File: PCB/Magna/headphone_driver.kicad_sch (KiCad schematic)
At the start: 36 parts, among them J1201 AudioJack3, U1201 NE5532, U1202 NE5532, U1203 TDA2822D

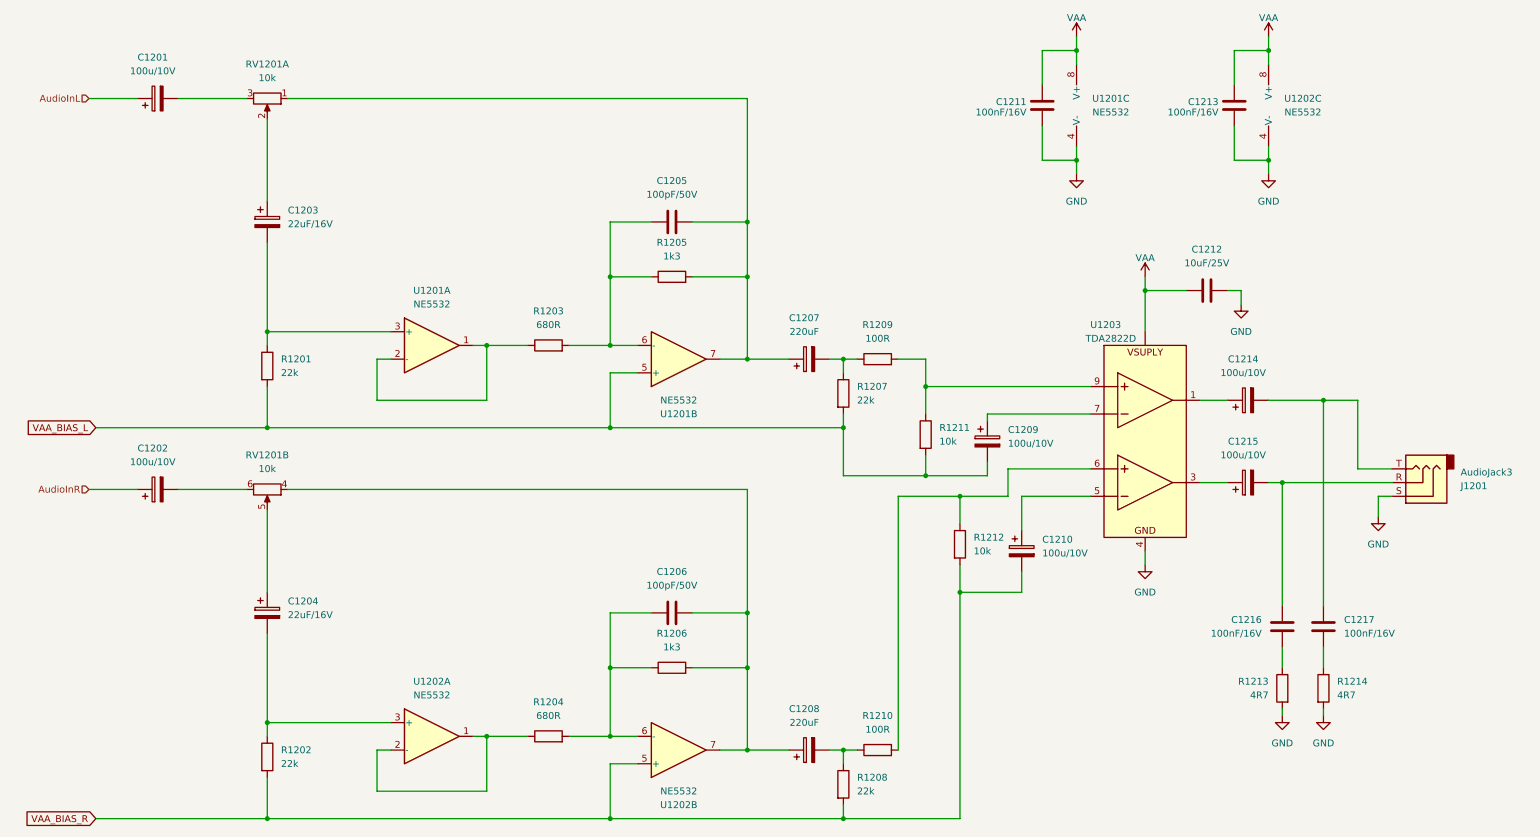
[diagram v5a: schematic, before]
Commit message: Add even more component footprints and partnumbers
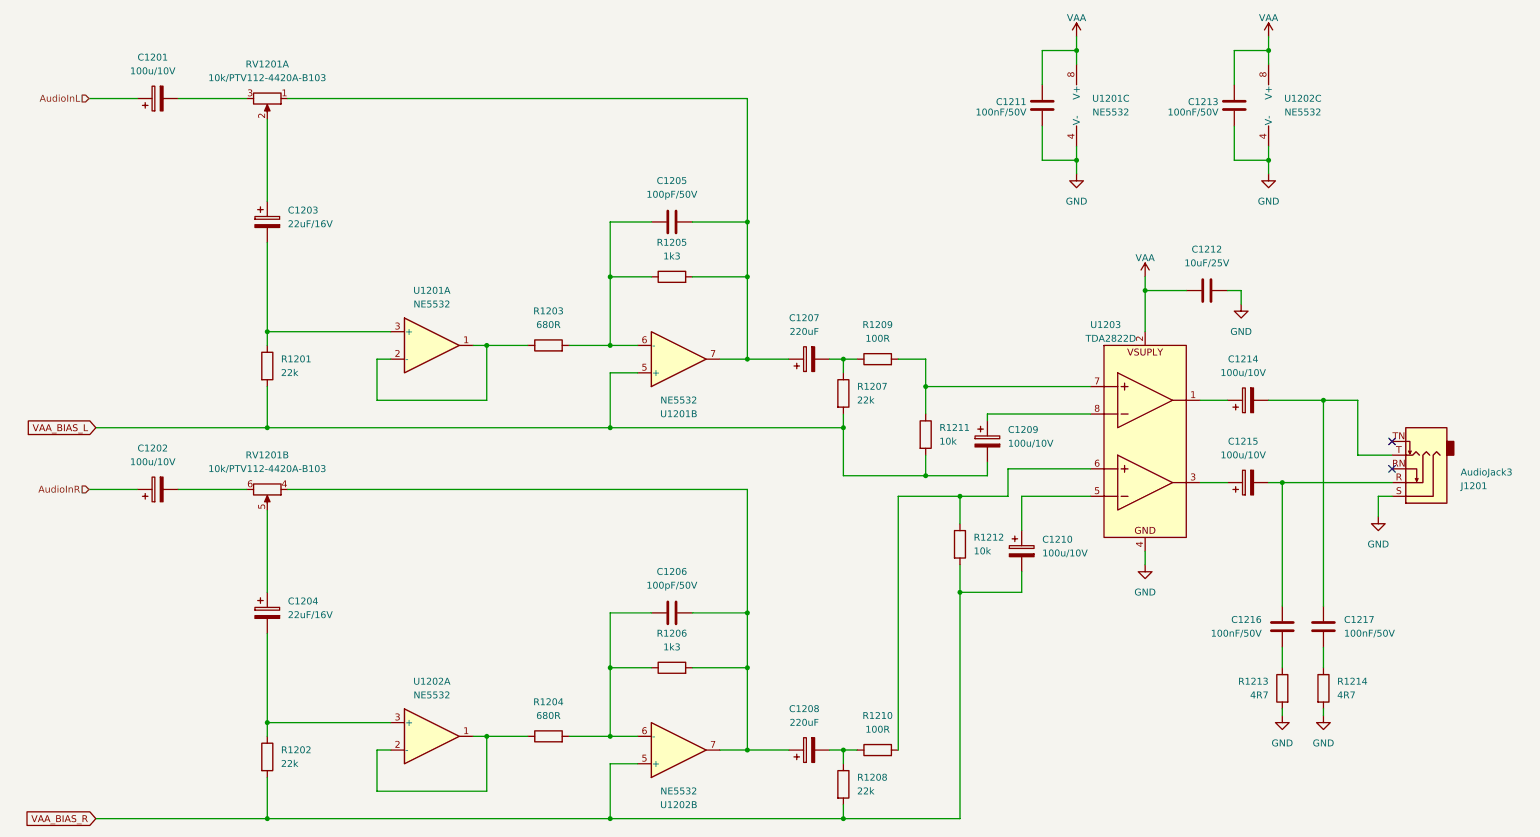
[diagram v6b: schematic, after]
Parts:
- C1205, C1206: footprint Capacitor_SMD:C_0805_2012Metric -> Capacitor_SMD:C_0805_2012Metric_Pad1.18x1.45mm_HandSolder
- C1211, C1213, C1216, C1217: value 100nF/16V -> 100nF/50V; footprint Capacitor_SMD:C_0805_2012Metric -> Capacitor_SMD:C_0805_2012Metric_Pad1.18x1.45mm_HandSolder; LCSC C218638 -> C49678
- J1201: symbol Connector_Audio:AudioJack3 -> Connector_Audio:AudioJack3_SwitchTR
- R1201, R1202, R1207, R1208, R1211, R1212: footprint Resistor_SMD:R_0805_2012Metric -> Resistor_SMD:R_0805_2012Metric_Pad1.20x1.40mm_HandSolder
- RV1201: value 10k -> 10k/PTV112-4420A-B103; footprint (none) -> Skrooter_footprints:Potentiometer_Bourns_PTV09A-1_Dual_Vertical
- U1201, U1202: footprint (none) -> Package_SO:SOIC-8_3.9x4.9mm_P1.27mm
- U1203: footprint (none) -> Package_SO:SOP-8_3.9x4.9mm_P1.27mm
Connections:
- net VAA: now also U1203.2 (VCC); no longer U1203. (VCC)
- net at C1209.1: now also U1203.8 (Input1+); no longer U1203.7 (Input1+)
- net at R1209.2, R1211.1: now also U1203.7 (Input1-); no longer U1203.9 (Input1-)
- no-connect marks 0 -> 2
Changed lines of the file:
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@@
   (junction (at 121.92 78.74) (diameter 0) (color 0 0 0 0)
   )
+  (no_connect (at 266.7 101.6))
+  (no_connect (at 266.7 96.52))
   (wire (pts (xy 62.23 33.02) (xy 147.32 33.02))
     (stroke (width 0) (type default))
@@
     (stroke (width 0) (type default))
   )
-  (wire (pts (xy 266.7 101.6) (xy 260.35 101.6))
-    (stroke (width 0) (type default))
-  )
   (wire (pts (xy 41.91 33.02) (xy 54.61 33.02))
     (stroke (width 0) (type default))
@@
     (stroke (width 0) (type default))
   )
-  (wire (pts (xy 260.35 88.9) (xy 260.35 101.6))
+  (wire (pts (xy 260.35 88.9) (xy 260.35 99.06))
     (stroke (width 0) (type default))
   )
@@
   )
   (wire (pts (xy 195.58 106.68) (xy 186.69 106.68))
+    (stroke (width 0) (type default))
+  )
+  (wire (pts (xy 260.35 99.06) (xy 266.7 99.06))
     (stroke (width 0) (type default))
   )
@@
       (effects (font (size 1.27 1.27)))
     )
-    (property "Value" "10k" (at 58.42 101.6 90)
-      (effects (font (size 1.27 1.27)))
-    )
-    (property "Footprint" "" (at 58.42 105.41 0)
+    (property "Value" "10k/PTV112-4420A-B103" (at 58.42 101.6 90)
+      (effects (font (size 1.27 1.27)))
+    )
+    (property "Footprint" "Skrooter_footprints:Potentiometer_Bourns_PTV09A-1_Dual_Vertical" (at 58.42 105.41 0)
       (effects (font (size 1.27 1.27)) hide)
     )
@@
     )
   )
-  (symbol (lib_id "Connector_Audio:AudioJack3") (at 271.78 104.14 180) (unit 1)
+  (symbol (lib_id "Connector_Audio:AudioJack3_SwitchTR") (at 271.78 104.14 180) (unit 1)
     (in_bom yes) (on_board yes) (dnp no)
     (property "Reference" "J1201" (at 279.4 104.775 0)
@@
     (pin "R")
     (pin "S")
+    (pin "RN")
+    (pin "TN")
     (instances
       (project "Magna"
@@
       (effects (font (size 1.27 1.27)) (justify left))
     )
-    (property "Footprint" "Resistor_SMD:R_0805_2012Metric" (at 56.642 82.55 90)
+    (property "Footprint" "Resistor_SMD:R_0805_2012Metric_Pad1.20x1.40mm_HandSolder" (at 56.642 82.55 90)
       (effects (font (size 1.27 1.27)) hide)
     )
@@
       (effects (font (size 1.27 1.27)))
     )
-    (property "Footprint" "" (at 88.9 78.74 0)
+    (property "Footprint" "Package_SO:SOIC-8_3.9x4.9mm_P1.27mm" (at 88.9 78.74 0)
       (effects (font (size 1.27 1.27)) hide)
     )
@@
       (effects (font (size 1.27 1.27)))
     )
-    (property "Value" "10k" (at 58.42 29.21 90)
-      (effects (font (size 1.27 1.27)))
-    )
-    (property "Footprint" "" (at 58.42 33.02 0)
+    (property "Value" "10k/PTV112-4420A-B103" (at 58.42 29.21 90)
+      (effects (font (size 1.27 1.27)))
+    )
+    (property "Footprint" "Skrooter_footprints:Potentiometer_Bourns_PTV09A-1_Dual_Vertical" (at 58.42 33.02 0)
       (effects (font (size 1.27 1.27)) hide)
     )
@@
       (effects (font (size 1.27 1.27)))
     )
-    (property "Footprint" "" (at 134.62 153.67 0)
+    (property "Footprint" "Package_SO:SOIC-8_3.9x4.9mm_P1.27mm" (at 134.62 153.67 0)
       (effects (font (size 1.27 1.27)) hide)
     )
@@
       (effects (font (size 1.27 1.27)) (justify left))
     )
-    (property "Footprint" "Resistor_SMD:R_0805_2012Metric" (at 163.322 87.63 90)
+    (property "Footprint" "Resistor_SMD:R_0805_2012Metric_Pad1.20x1.40mm_HandSolder" (at 163.322 87.63 90)
       (effects (font (size 1.27 1.27)) hide)
     )
@@
       (effects (font (size 1.27 1.27)) (justify left))
     )
-    (property "Footprint" "Resistor_SMD:R_0805_2012Metric" (at 163.322 160.02 90)
+    (property "Footprint" "Resistor_SMD:R_0805_2012Metric_Pad1.20x1.40mm_HandSolder" (at 163.322 160.02 90)
       (effects (font (size 1.27 1.27)) hide)
     )
@@
       (effects (font (size 1.27 1.27)) (justify left))
     )
-    (property "Footprint" "Resistor_SMD:R_0805_2012Metric" (at 184.912 115.57 90)
+    (property "Footprint" "Resistor_SMD:R_0805_2012Metric_Pad1.20x1.40mm_HandSolder" (at 184.912 115.57 90)
       (effects (font (size 1.27 1.27)) hide)
     )
@@
       (effects (font (size 1.27 1.27)) (justify left))
     )
-    (property "Footprint" "Resistor_SMD:R_0805_2012Metric" (at 56.642 154.94 90)
+    (property "Footprint" "Resistor_SMD:R_0805_2012Metric_Pad1.20x1.40mm_HandSolder" (at 56.642 154.94 90)
       (effects (font (size 1.27 1.27)) hide)
     )
@@
       (effects (font (size 1.27 1.27)))
     )
-    (property "Footprint" "" (at 134.62 81.28 0)
+    (property "Footprint" "Package_SO:SOIC-8_3.9x4.9mm_P1.27mm" (at 134.62 81.28 0)
       (effects (font (size 1.27 1.27)) hide)
     )
@@
       (effects (font (size 1.27 1.27)))
     )
-    (property "Footprint" "Capacitor_SMD:C_0805_2012Metric" (at 137.16 54.9148 0)
+    (property "Footprint" "Capacitor_SMD:C_0805_2012Metric_Pad1.18x1.45mm_HandSolder" (at 137.16 54.9148 0)
       (effects (font (size 1.27 1.27)) hide)
     )
@@
       (effects (font (size 1.27 1.27)))
     )
-    (property "Footprint" "" (at 246.38 34.29 0)
+    (property "Footprint" "Package_SO:SOIC-8_3.9x4.9mm_P1.27mm" (at 246.38 34.29 0)
       (effects (font (size 1.27 1.27)) hide)
     )
@@
       (effects (font (size 1.27 1.27)))
     )
-    (property "Footprint" "Capacitor_SMD:C_0805_2012Metric" (at 137.16 127.3048 0)
+    (property "Footprint" "Capacitor_SMD:C_0805_2012Metric_Pad1.18x1.45mm_HandSolder" (at 137.16 127.3048 0)
       (effects (font (size 1.27 1.27)) hide)
     )
@@
       (effects (font (size 1.27 1.27)) (justify left))
     )
-    (property "Footprint" "Resistor_SMD:R_0805_2012Metric" (at 178.562 95.25 90)
+    (property "Footprint" "Resistor_SMD:R_0805_2012Metric_Pad1.20x1.40mm_HandSolder" (at 178.562 95.25 90)
       (effects (font (size 1.27 1.27)) hide)
     )
@@
       (effects (font (size 1.27 1.27)))
     )
-    (property "Footprint" "" (at 210.82 34.29 0)
+    (property "Footprint" "Package_SO:SOIC-8_3.9x4.9mm_P1.27mm" (at 210.82 34.29 0)
       (effects (font (size 1.27 1.27)) hide)
     )
@@
       (effects (font (size 1.27 1.27)) (justify left))
     )
-    (property "Value" "100nF/16V" (at 242.57 132.08 0)
-      (effects (font (size 1.27 1.27)) (justify left))
-    )
-    (property "Footprint" "Capacitor_SMD:C_0805_2012Metric" (at 245.4148 134.62 0)
+    (property "Value" "100nF/50V" (at 242.57 132.08 0)
+      (effects (font (size 1.27 1.27)) (justify left))
+    )
+    (property "Footprint" "Capacitor_SMD:C_0805_2012Metric_Pad1.18x1.45mm_HandSolder" (at 245.4148 134.62 0)
       (effects (font (size 1.27 1.27)) hide)
     )
@@
       (effects (font (size 1.27 1.27)) hide)
     )
-    (property "LCSC" "C218638" (at 246.38 130.81 0)
+    (property "LCSC" "C49678" (at 246.38 130.81 0)
       (effects (font (size 1.27 1.27)) hide)
     )
@@
       (effects (font (size 1.27 1.27)) (justify left))
     )
-    (property "Value" "100nF/16V" (at 199.009 35.5673 0)
-      (effects (font (size 1.27 1.27)) (justify left))
-    )
-    (property "Footprint" "Capacitor_SMD:C_0805_2012Metric" (at 200.9648 38.1 0)
+    (property "Value" "100nF/50V" (at 199.009 35.5673 0)
+      (effects (font (size 1.27 1.27)) (justify left))
+    )
+    (property "Footprint" "Capacitor_SMD:C_0805_2012Metric_Pad1.18x1.45mm_HandSolder" (at 200.9648 38.1 0)
       (effects (font (size 1.27 1.27)) hide)
     )
@@
       (effects (font (size 1.27 1.27)) hide)
     )
-    (property "LCSC" "C218638" (at 201.93 34.29 0)
+    (property "LCSC" "C49678" (at 201.93 34.29 0)
       (effects (font (size 1.27 1.27)) hide)
     )
@@
       (effects (font (size 1.27 1.27)))
     )
-    (property "Footprint" "" (at 213.36 86.36 0)
+    (property "Footprint" "Package_SO:SOP-8_3.9x4.9mm_P1.27mm" (at 213.36 86.36 0)
       (effects (font (size 1.27 1.27)) hide)
     )
@@
     (pin "1")
     (pin "4")
-    (pin "")
+    (pin "2")
     (pin "7")
-    (pin "9")
+    (pin "8")
     (pin "3")
     (pin "5")
@@
       (effects (font (size 1.27 1.27)) (justify left))
     )
-    (property "Value" "100nF/16V" (at 257.81 132.08 0)
-      (effects (font (size 1.27 1.27)) (justify left))
-    )
-    (property "Footprint" "Capacitor_SMD:C_0805_2012Metric" (at 254.9652 134.62 0)
+    (property "Value" "100nF/50V" (at 257.81 132.08 0)
+      (effects (font (size 1.27 1.27)) (justify left))
+    )
+    (property "Footprint" "Capacitor_SMD:C_0805_2012Metric_Pad1.18x1.45mm_HandSolder" (at 254.9652 134.62 0)
       (effects (font (size 1.27 1.27)) hide)
     )
@@
       (effects (font (size 1.27 1.27)) hide)
     )
-    (property "LCSC" "C218638" (at 254 130.81 0)
+    (property "LCSC" "C49678" (at 254 130.81 0)
       (effects (font (size 1.27 1.27)) hide)
     )
@@
       (effects (font (size 1.27 1.27)))
     )
-    (property "Footprint" "" (at 88.9 151.13 0)
+    (property "Footprint" "Package_SO:SOIC-8_3.9x4.9mm_P1.27mm" (at 88.9 151.13 0)
       (effects (font (size 1.27 1.27)) hide)
     )
@@
       (effects (font (size 1.27 1.27)) (justify left))
     )
-    (property "Value" "100nF/16V" (at 234.569 35.5673 0)
-      (effects (font (size 1.27 1.27)) (justify left))
-    )
-    (property "Footprint" "Capacitor_SMD:C_0805_2012Metric" (at 236.5248 38.1 0)
+    (property "Value" "100nF/50V" (at 234.569 35.5673 0)
+      (effects (font (size 1.27 1.27)) (justify left))
+    )
+    (property "Footprint" "Capacitor_SMD:C_0805_2012Metric_Pad1.18x1.45mm_HandSolder" (at 236.5248 38.1 0)
       (effects (font (size 1.27 1.27)) hide)
     )
@@
       (effects (font (size 1.27 1.27)) hide)
     )
-    (property "LCSC" "C218638" (at 237.49 34.29 0)
-      (effects (font (size 1.27 1.27)) hide)
-    )
+    (property "LCSC" "C49678" (at 237.49 34.29 0)
+      (effects (font (size 1.27 1.27)) hide)
+    )
